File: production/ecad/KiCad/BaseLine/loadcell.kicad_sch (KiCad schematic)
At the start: 17 parts, among them J4 LoadCellConnector, J9 ConnToESP32, U11 TXB0104DR, U6 MIC920YC5-TR, U7 MIC920YC5-TR, U8 ADS1231IDR

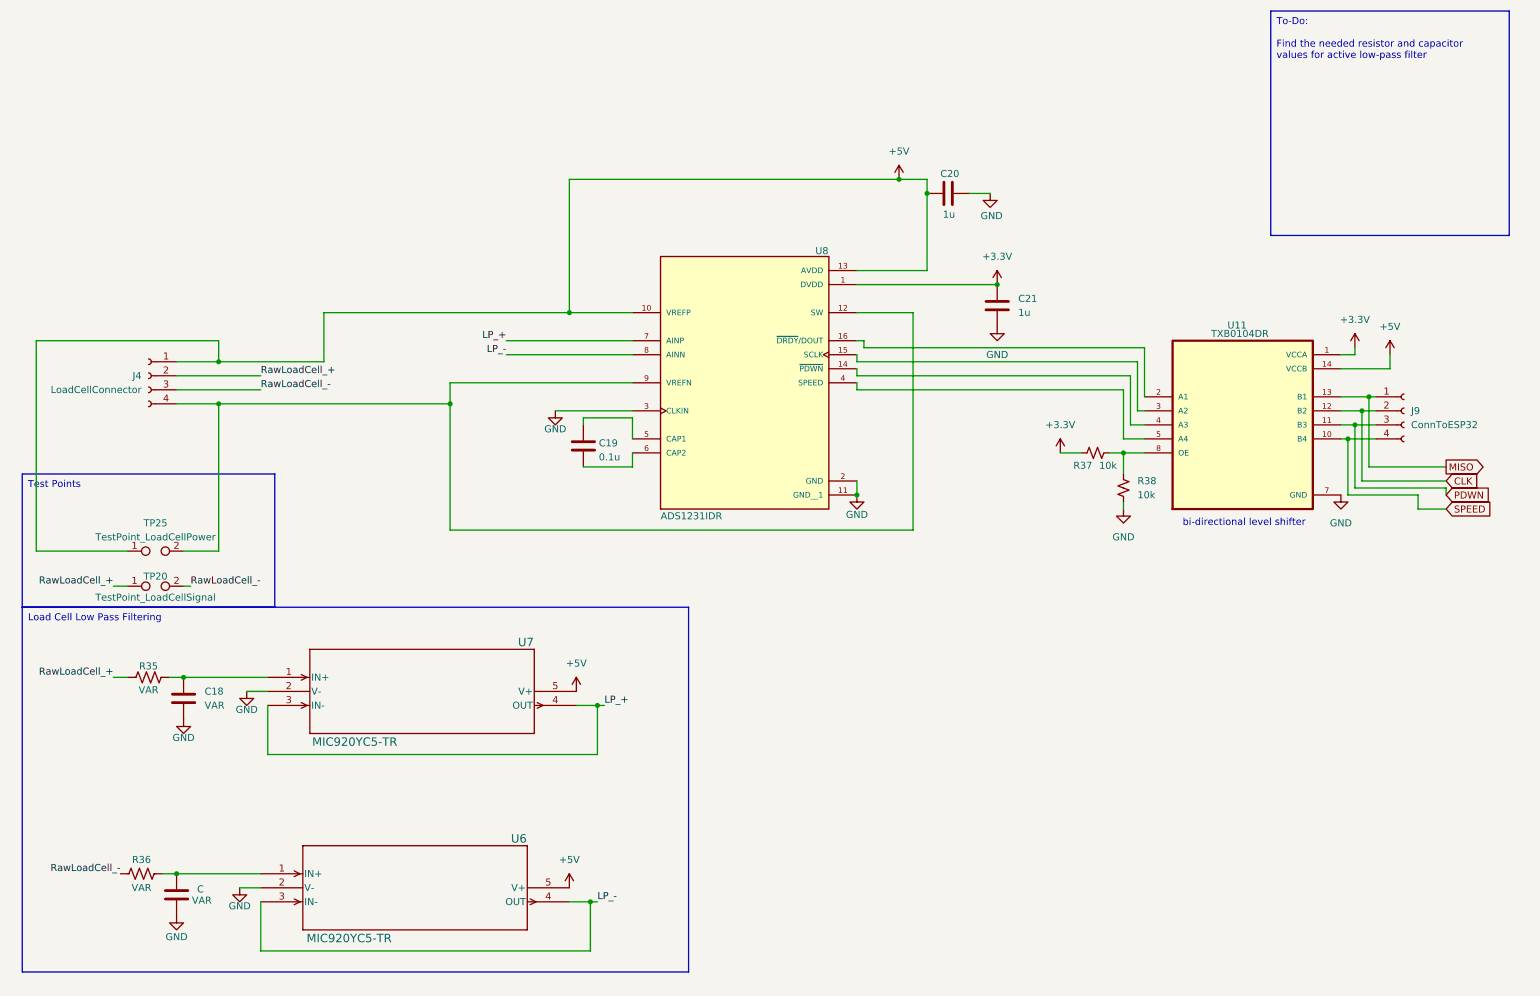
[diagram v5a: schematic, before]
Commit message: Load cell updates
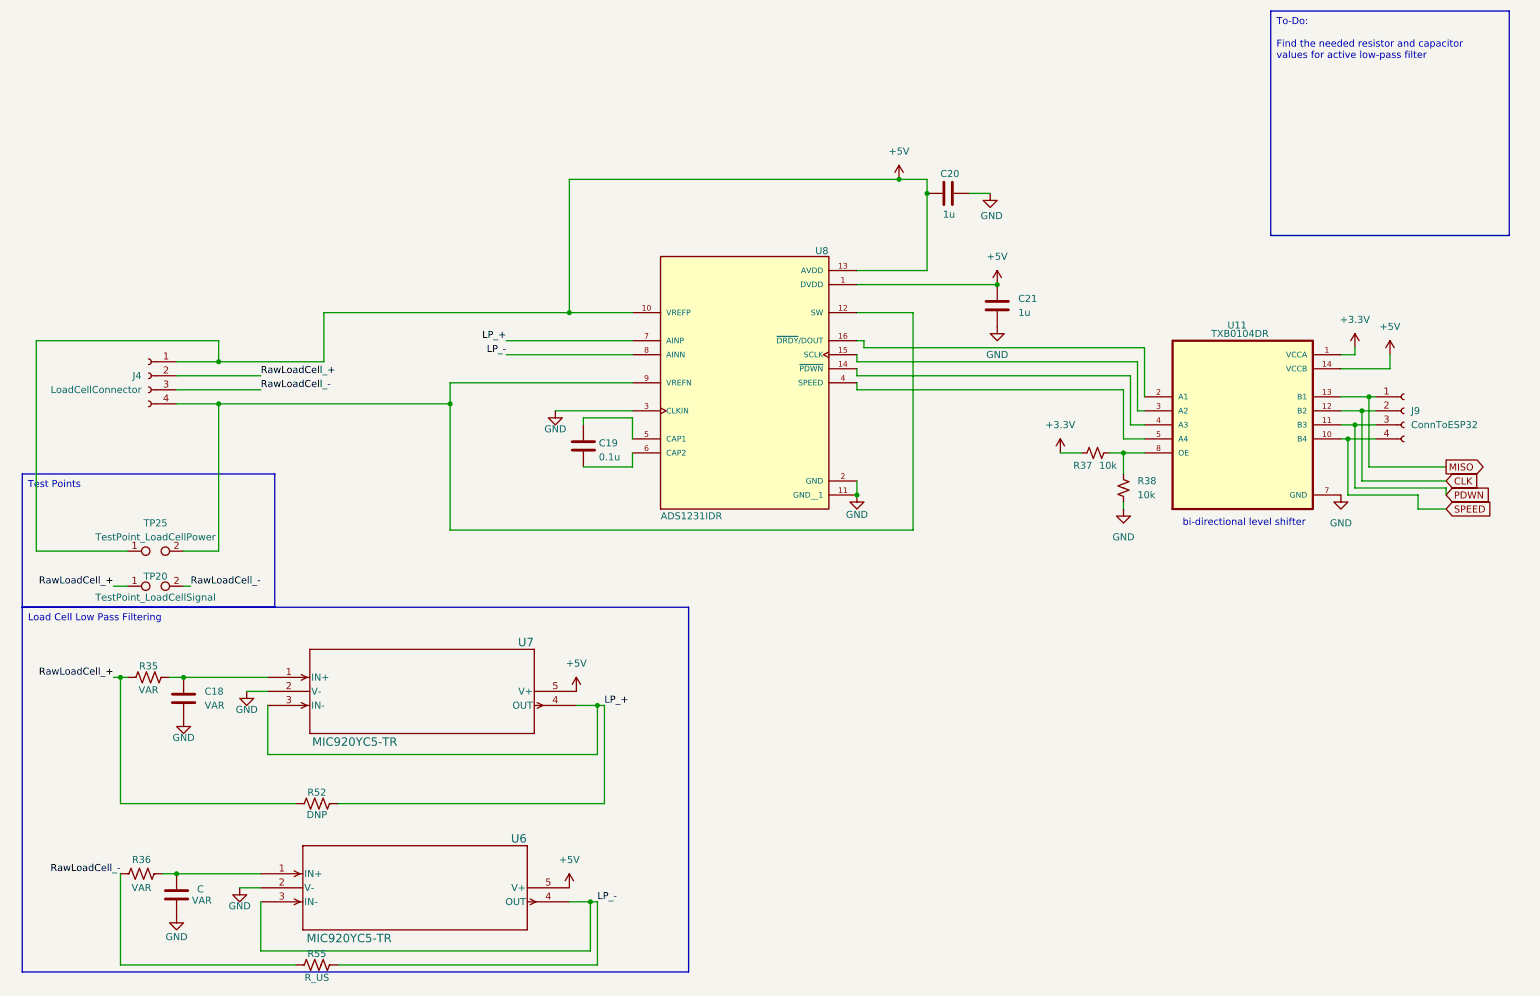
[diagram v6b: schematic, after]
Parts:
- added R52: DNP, symbol Device:R_US
- added R55: R_US, symbol Device:R_US
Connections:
- net +3.3V: no longer C21.1, U8.1 (DVDD)
- net +5V: now also C21.1, U8.1 (DVDD)
- net LP_+: now also R52.1
- net LP_-: now also R55.1
- net RawLoadCell_+: now also R52.2
- net RawLoadCell_-: now also R55.2
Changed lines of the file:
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@@
 	)
 	(junction
+		(at 31.75 142.24)
+		(diameter 0)
+		(color 0 0 0 0)
+	)
+	(junction
 		(at 91.44 92.71)
 		(diameter 0)
@@
 	)
 	(junction
-		(at 190.5 71.12)
+		(at 116.84 182.88)
 		(diameter 0)
 		(color 0 0 0 0)
 	)
 	(junction
-		(at 116.84 182.88)
+		(at 190.5 71.12)
 		(diameter 0)
 		(color 0 0 0 0)
@@
 	(wire
 		(pts
+			(xy 31.75 142.24) (xy 31.75 165.1)
+		)
+		(stroke
+			(width 0)
+			(type default)
+		)
+	)
+	(wire
+		(pts
 			(xy 114.3 147.32) (xy 118.11 147.32)
 		)
@@
 	(wire
 		(pts
+			(xy 31.75 194.31) (xy 31.75 177.8)
+		)
+		(stroke
+			(width 0)
+			(type default)
+		)
+	)
+	(wire
+		(pts
 			(xy 118.11 147.32) (xy 118.11 156.21)
 		)
@@
 	(wire
 		(pts
-			(xy 30.48 142.24) (xy 33.02 142.24)
+			(xy 30.48 142.24) (xy 31.75 142.24)
 		)
 		(stroke
@@
 	(wire
 		(pts
+			(xy 63.5 194.31) (xy 31.75 194.31)
+		)
+		(stroke
+			(width 0)
+			(type default)
+		)
+	)
+	(wire
+		(pts
 			(xy 116.84 182.88) (xy 116.84 191.77)
 		)
@@
 	(wire
 		(pts
+			(xy 71.12 165.1) (xy 119.38 165.1)
+		)
+		(stroke
+			(width 0)
+			(type default)
+		)
+	)
+	(wire
+		(pts
 			(xy 252.73 93.98) (xy 256.54 93.98)
 		)
@@
 	(wire
 		(pts
+			(xy 31.75 165.1) (xy 63.5 165.1)
+		)
+		(stroke
+			(width 0)
+			(type default)
+		)
+	)
+	(wire
+		(pts
 			(xy 255.27 83.82) (xy 255.27 82.55)
 		)
@@
 	(wire
 		(pts
+			(xy 118.11 194.31) (xy 118.11 182.88)
+		)
+		(stroke
+			(width 0)
+			(type default)
+		)
+	)
+	(wire
+		(pts
+			(xy 119.38 165.1) (xy 119.38 147.32)
+		)
+		(stroke
+			(width 0)
+			(type default)
+		)
+	)
+	(wire
+		(pts
+			(xy 71.12 194.31) (xy 118.11 194.31)
+		)
+		(stroke
+			(width 0)
+			(type default)
+		)
+	)
+	(wire
+		(pts
 			(xy 175.26 76.2) (xy 175.26 115.57)
 		)
@@
 	(wire
 		(pts
+			(xy 31.75 142.24) (xy 33.02 142.24)
+		)
+		(stroke
+			(width 0)
+			(type default)
+		)
+	)
+	(wire
+		(pts
 			(xy 256.54 93.98) (xy 259.08 93.98)
 		)
@@
 	)
 	(symbol
+		(lib_id "Device:R_US")
+		(at 67.31 165.1 270)
+		(unit 1)
+		(exclude_from_sim no)
+		(in_bom yes)
+		(on_board yes)
+		(dnp no)
+		(property "Reference" "R52"
+			(at 67.31 163.068 90)
+			(effects
+				(font
+					(size 1.27 1.27)
+				)
+			)
+		)
+		(property "Value" "DNP"
+			(at 67.31 167.132 90)
+			(effects
+				(font
+					(size 1.27 1.27)
+				)
+			)
+		)
+		(property "Footprint" ""
+			(at 67.056 166.116 90)
+			(effects
+				(font
+					(size 1.27 1.27)
+				)
+				(hide yes)
+			)
+		)
+		(property "Datasheet" "~"
+			(at 67.31 165.1 0)
+			(effects
+				(font
+					(size 1.27 1.27)
+				)
+				(hide yes)
+			)
+		)
+		(property "Description" "Resistor, US symbol"
+			(at 67.31 165.1 0)
+			(effects
+				(font
+					(size 1.27 1.27)
+				)
+				(hide yes)
+			)
+		)
+		(pin "2"
+		)
+		(pin "1"
+		)
+		(instances
+			(project "BaseLine"
+				(path "/ba9eda21-3882-41e1-8265-3d8ac781da20/15451660-bad9-4e79-85d3-2d59df8c5ccd"
+					(reference "R52")
+					(unit 1)
+				)
+			)
+		)
+	)
+	(symbol
 		(lib_name "MIC920YC5-TR_1")
 		(lib_id "2024-10-08_01-43-59:MIC920YC5-TR")
@@
 	)
 	(symbol
-		(lib_id "power:+3.3V")
-		(at 190.5 71.12 0)
-		(unit 1)
-		(exclude_from_sim no)
-		(in_bom yes)
-		(on_board yes)
-		(dnp no)
-		(fields_autoplaced yes)
-		(property "Reference" "#PWR060"
-			(at 190.5 74.93 0)
-			(effects
-				(font
-					(size 1.27 1.27)
-				)
-				(hide yes)
-			)
-		)
-		(property "Value" "+3.3V"
-			(at 190.5 66.04 0)
-			(effects
-				(font
-					(size 1.27 1.27)
-				)
-			)
-		)
-		(property "Footprint" ""
-			(at 190.5 71.12 0)
-			(effects
-				(font
-					(size 1.27 1.27)
-				)
-				(hide yes)
-			)
-		)
-		(property "Datasheet" ""
-			(at 190.5 71.12 0)
-			(effects
-				(font
-					(size 1.27 1.27)
-				)
-				(hide yes)
-			)
-		)
-		(property "Description" "Power symbol creates a global label with name \"+3.3V\""
-			(at 190.5 71.12 0)
-			(effects
-				(font
-					(size 1.27 1.27)
-				)
-				(hide yes)
-			)
-		)
-		(pin "1"
-		)
-		(instances
-			(project "BaseLine"
-				(path "/ba9eda21-3882-41e1-8265-3d8ac781da20/15451660-bad9-4e79-85d3-2d59df8c5ccd"
-					(reference "#PWR060")
-					(unit 1)
-				)
-			)
-		)
-	)
-	(symbol
 		(lib_id "power:GND")
 		(at 190.5 78.74 0)
@@
 	(symbol
 		(lib_id "power:+5V")
+		(at 190.5 71.12 0)
+		(unit 1)
+		(exclude_from_sim no)
+		(in_bom yes)
+		(on_board yes)
+		(dnp no)
+		(property "Reference" "#PWR060"
+			(at 190.5 74.93 0)
+			(effects
+				(font
+					(size 1.27 1.27)
+				)
+				(hide yes)
+			)
+		)
+		(property "Value" "+5V"
+			(at 190.5 66.04 0)
+			(effects
+				(font
+					(size 1.27 1.27)
+				)
+			)
+		)
+		(property "Footprint" ""
+			(at 190.5 71.12 0)
+			(effects
+				(font
+					(size 1.27 1.27)
+				)
+				(hide yes)
+			)
+		)
+		(property "Datasheet" ""
+			(at 190.5 71.12 0)
+			(effects
+				(font
+					(size 1.27 1.27)
+				)
+				(hide yes)
+			)
+		)
+		(property "Description" "Power symbol creates a global label with name \"+5V\""
+			(at 190.5 71.12 0)
+			(effects
+				(font
+					(size 1.27 1.27)
+				)
+				(hide yes)
+			)
+		)
+		(pin "1"
+		)
+		(instances
+			(project "BaseLine"
+				(path "/ba9eda21-3882-41e1-8265-3d8ac781da20/15451660-bad9-4e79-85d3-2d59df8c5ccd"
+					(reference "#PWR060")
+					(unit 1)
+				)
+			)
+		)
+	)
+	(symbol
+		(lib_id "power:+5V")
 		(at 113.03 180.34 0)
 		(unit 1)
@@
 					(unit 1)
 				)
+			)
+		)
+	)
+	(symbol
+		(lib_id "Device:R_US")
+		(at 67.31 194.31 270)
+		(unit 1)
+		(exclude_from_sim no)
+		(in_bom yes)
+		(on_board yes)
+		(dnp no)
+		(property "Reference" "R55"
+			(at 67.31 192.278 90)
+			(effects
+				(font
+					(size 1.27 1.27)
+				)
+			)
+		)
+		(property "Value" "R_US"
+			(at 67.31 196.596 90)
+			(effects
+				(font
+					(size 1.27 1.27)
+				)
+			)
+		)
+		(property "Footprint" ""
+			(at 67.056 195.326 90)
+			(effects
+				(font
+					(size 1.27 1.27)
+				)
+				(hide yes)
+			)
+		)
+		(property "Datasheet" "~"
+			(at 67.31 194.31 0)
+			(effects
+				(font
+					(size 1.27 1.27)
+				)
+				(hide yes)
+			)
+		)
+		(property "Description" "Resistor, US symbol"
+			(at 67.31 194.31 0)
+			(effects
+				(font
+					(size 1.27 1.27)
+				)
+				(hide yes)
+			)
+		)
+		(pin "2"
+		)
+		(pin "1"
+		)
+		(instances
+			(project "BaseLine"
+				(path "/ba9eda21-3882-41e1-8265-3d8ac781da20/15451660-bad9-4e79-85d3-2d59df8c5ccd"
+					(reference "R55")
+					(unit 1)
+				)

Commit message: Final mux changes
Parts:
- R55: value R_US -> DNP
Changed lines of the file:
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@@
 			)
 		)
-		(property "Value" "R_US"
+		(property "Value" "DNP"
 			(at 67.31 196.596 90)
 			(effects

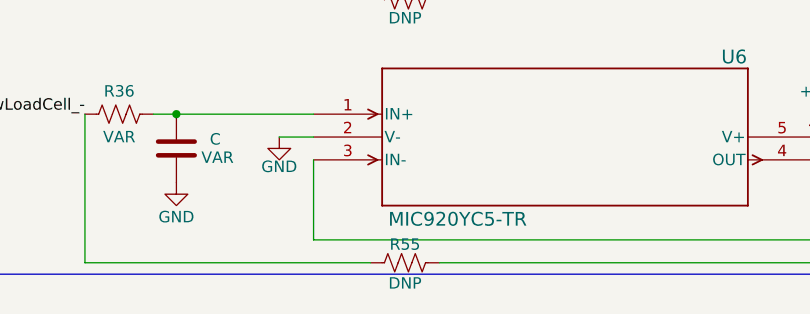
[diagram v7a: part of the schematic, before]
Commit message: Updated more footprints
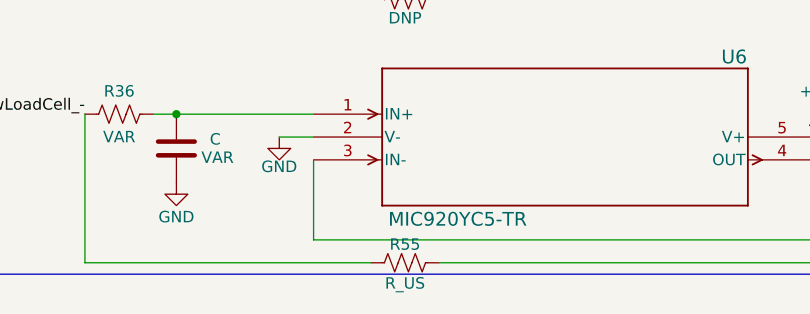
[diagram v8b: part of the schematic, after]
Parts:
- R55: value DNP -> R_US
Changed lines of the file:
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@@
 			)
 		)
-		(property "Value" "DNP"
+		(property "Value" "R_US"
 			(at 67.31 196.596 90)
 			(effects
